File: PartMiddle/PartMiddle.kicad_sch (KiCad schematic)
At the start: 14 parts, among them J1 MiddleHalf, J2 Middle, SW1 SW_Push, SW2 SW_Push, SW3 SW_Push, SW4 SW_Push, SW5 SW_Push, SW6 SW_Push

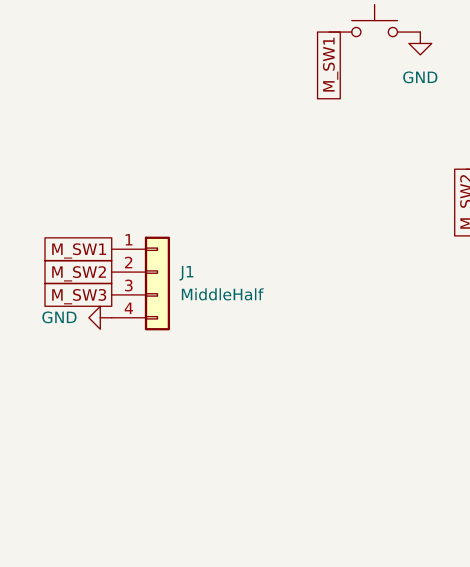
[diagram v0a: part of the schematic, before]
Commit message: Realign middle part pings to the right part.
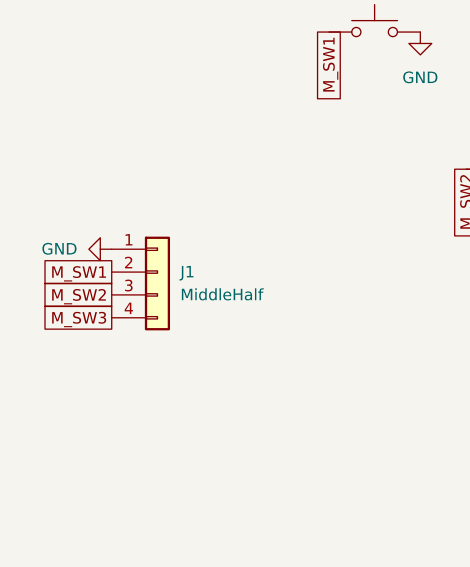
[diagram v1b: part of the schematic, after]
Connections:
- net GND: now also J1.1 (Pin_1); no longer J1.4 (Pin_4)
- net M_SW1: now also J1.2 (Pin_2); no longer J1.1 (Pin_1)
- net M_SW2: now also J1.3 (Pin_3); no longer J1.2 (Pin_2)
- net M_SW3: now also J1.4 (Pin_4); no longer J1.3 (Pin_3)
